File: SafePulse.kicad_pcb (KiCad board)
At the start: 4 copper layers, 40.6 x 20.8 mm, 88 parts, among them IC1 S-35770E01I-K8T2U, J1 Conn_01x03_Male, J2 4208, Q1 FQT7N10L, Q2 BC846A, Q3 MMBT3906, Q4 MMBT3906, U1 TS4061AICT-1.25, U2 74HC14, U3 TLV27L1DBVT, U33 MAX9910EXK+T, U4 CD14538BM

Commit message: added Allan changes
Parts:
- U1: footprint Package_TO_SOT_SMD:SOT-323_SC-70 -> Package_TO_SOT_SMD:SOT-23

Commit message: Updated V1.2.4 board with new JCLPCB number
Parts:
- Q1: footprint Package_TO_SOT_SMD:SOT-223-3_TabPin4 -> Library:SOT230P700X180-4N
- U1: footprint Package_TO_SOT_SMD:SOT-23 -> Library:SOT65P210X110-3N
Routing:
- net GND: track 64.3 -> 63.6 mm
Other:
- copper layers 4 -> 13

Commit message: V1.2.5 boards
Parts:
- Q1: footprint Library:SOT230P700X180-4N -> Package_TO_SOT_SMD:SOT-223-3_TabPin4
- Q2: footprint Package_TO_SOT_SMD:SOT-23 -> Package_TO_SOT_SMD:SOT-323_SC-70_Handsoldering
- U1: footprint Library:SOT65P210X110-3N -> Package_TO_SOT_SMD:SOT-23
- moved Q2 0.51 mm to (149.9, 72.7)
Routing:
- net GND: track 63.6 -> 64.9 mm

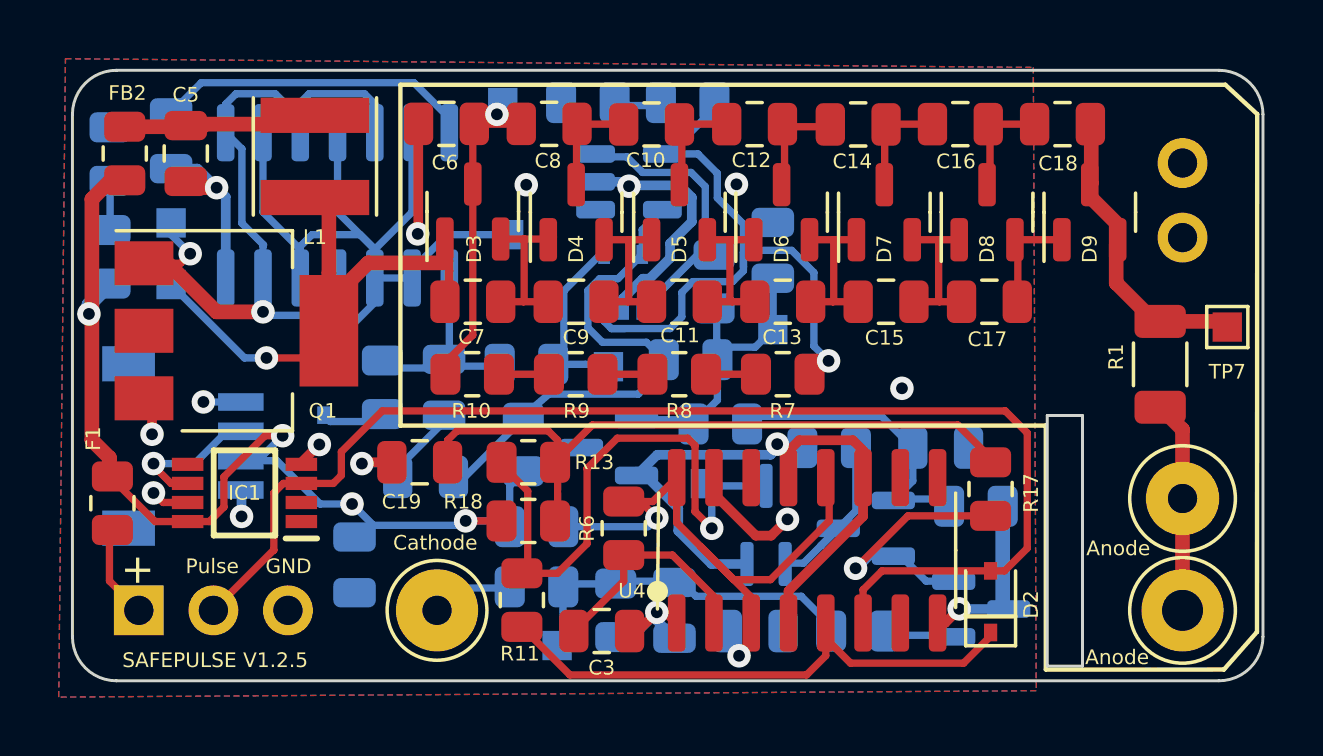
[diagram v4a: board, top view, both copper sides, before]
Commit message: Update layout for SOT-323 for U1 from a SOT-23 footprint
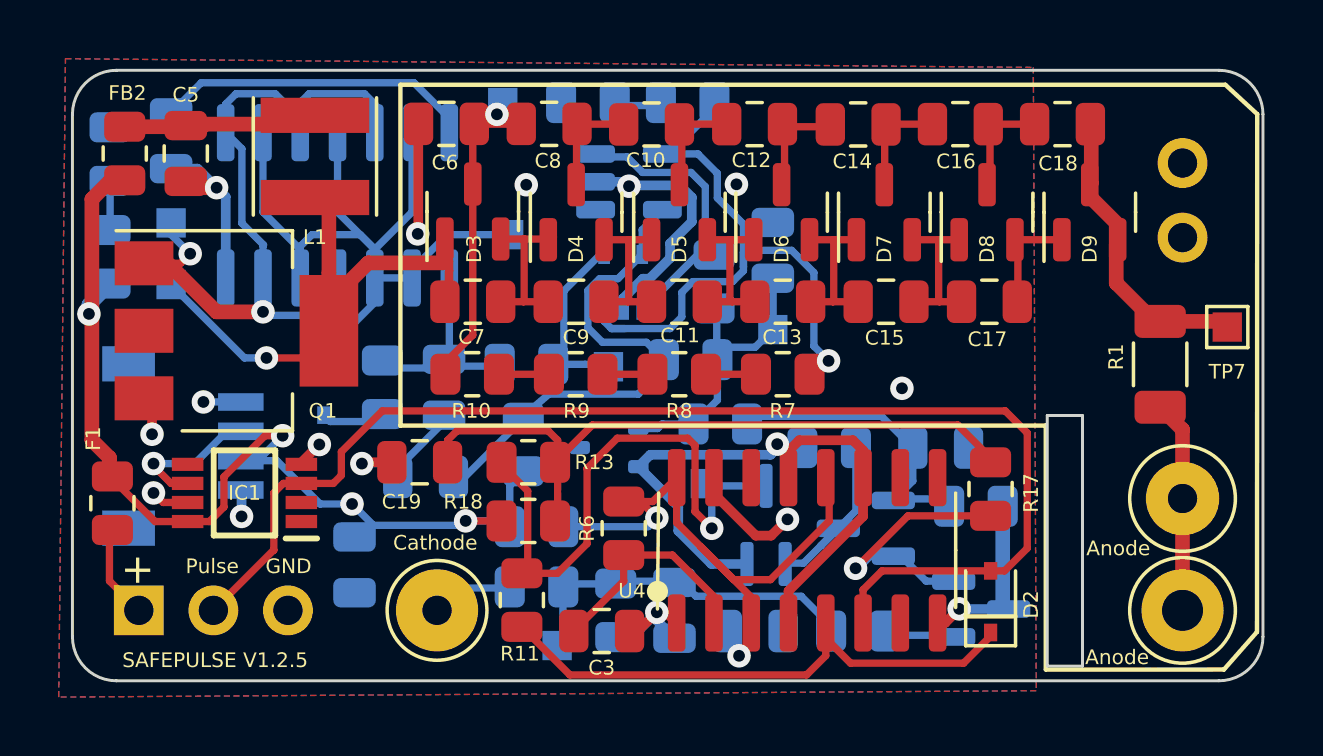
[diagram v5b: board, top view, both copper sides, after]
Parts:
- U1: footprint Package_TO_SOT_SMD:SOT-23 -> Package_TO_SOT_SMD:SOT-323_SC-70
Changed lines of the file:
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@@
 		)
 	)
-	(footprint "Package_TO_SOT_SMD:SOT-23"
+	(footprint "Package_TO_SOT_SMD:SOT-323_SC-70"
 		(layer "B.Cu")
 		(at 144.52 70.02 180)
-		(descr "SOT, 3 Pin (https://www.jedec.org/system/files/docs/to-236h.pdf variant AB), generated with kicad-footprint-generator ipc_gullwing_generator.py")
-		(tags "SOT TO_SOT_SMD")
+		(descr "SOT-323, SC-70")
+		(tags "SOT-323 SC-70")
 		(property "Reference" "U1"
-			(at 0 -2.055 0)
+			(at -0.05 2.25 0)
 			(layer "B.SilkS")
 			(effects
 				(font
-					(size 0.5 0.5)
-					(thickness 0.075)
+					(size 1 1)
+					(thickness 0.15)
 				)
 				(justify mirror)
@@
 		)
 		(property "Value" "TS4061AICT-1.25"
-			(at 0 -2.4 0)
+			(at -0.05 -2.05 0)
 			(layer "B.Fab")
-			(hide yes)
 			(effects
 				(font
@@
 			)
 		)
-		(property "Footprint" "Package_TO_SOT_SMD:SOT-23"
+		(property "Footprint" "Package_TO_SOT_SMD:SOT-323_SC-70"
 			(at 0 0 0)
 			(unlocked yes)
@@
 		(attr smd)
 		(fp_line
-			(start 0.65 1.56)
-			(end 0 1.56)
+			(start 0.73 1.16)
+			(end -0.68 1.16)
 			(stroke
 				(width 0.12)
@@
 		)
 		(fp_line
-			(start 0.65 -1.56)
-			(end 0 -1.56)
+			(start 0.73 0.5)
+			(end 0.73 1.16)
 			(stroke
 				(width 0.12)
@@
 		)
 		(fp_line
-			(start -0.65 1.56)
-			(end 0 1.56)
+			(start 0.73 -1.16)
+			(end 0.73 -0.5)
 			(stroke
 				(width 0.12)
@@
 		)
 		(fp_line
-			(start -0.65 -1.56)
-			(end 0 -1.56)
+			(start 0.73 -1.16)
+			(end -0.68 -1.16)
 			(stroke
 				(width 0.12)
@@
 		(fp_poly
 			(pts
-				(xy -1.1625 1.51) (xy -1.4025 1.84) (xy -0.9225 1.84) (xy -1.1625 1.51)
+				(xy -1.05 1.14) (xy -1.29 1.47) (xy -0.81 1.47) (xy -1.05 1.14)
 			)
 			(stroke
@@
 		)
 		(fp_line
-			(start 1.92 1.7)
-			(end 1.92 -1.7)
+			(start 1.7 1.3)
+			(end -1.7 1.3)
 			(stroke
 				(width 0.05)
@@
 		)
 		(fp_line
-			(start 1.92 -1.7)
-			(end -1.92 -1.7)
+			(start 1.7 -1.3)
+			(end 1.7 1.3)
 			(stroke
 				(width 0.05)
@@
 		)
 		(fp_line
-			(start -1.92 1.7)
-			(end 1.92 1.7)
+			(start -1.7 1.3)
+			(end -1.7 -1.3)
 			(stroke
 				(width 0.05)
@@
 		)
 		(fp_line
-			(start -1.92 -1.7)
-			(end -1.92 1.7)
+			(start -1.7 -1.3)
+			(end 1.7 -1.3)
 			(stroke
 				(width 0.05)
@@
 		)
 		(fp_line
-			(start 0.65 1.45)
-			(end -0.325 1.45)
+			(start 0.67 -1.1)
+			(end 0.67 1.1)
 			(stroke
 				(width 0.1)
@@
 		)
 		(fp_line
-			(start 0.65 -1.45)
-			(end 0.65 1.45)
+			(start -0.18 1.1)
+			(end 0.67 1.1)
 			(stroke
 				(width 0.1)
@@
 		)
 		(fp_line
-			(start -0.325 1.45)
-			(end -0.65 1.125)
+			(start -0.68 0.6)
+			(end -0.18 1.1)
 			(stroke
 				(width 0.1)
@@
 		)
 		(fp_line
-			(start -0.65 1.125)
-			(end -0.65 -1.45)
+			(start -0.68 -1.1)
+			(end 0.67 -1.1)
 			(stroke
 				(width 0.1)
@@
 		)
 		(fp_line
-			(start -0.65 -1.45)
-			(end 0.65 -1.45)
+			(start -0.68 -1.1)
+			(end -0.68 0.6)
 			(stroke
 				(width 0.1)
@@
 		)
 		(fp_text user "${REFERENCE}"
-			(at 0 0 0)
+			(at 0 0 90)
 			(layer "B.Fab")
 			(effects
 				(font
-					(size 0.32 0.32)
-					(thickness 0.05)
+					(size 0.5 0.5)
+					(thickness 0.075)
 				)
 				(justify mirror)
@@
 		)
 		(pad "1" smd roundrect
-			(at -0.9375 0.95 180)
-			(size 1.475 0.6)
+			(at -1 0.65 270)
+			(size 0.45 0.7)
 			(layers "B.Cu" "B.Paste" "B.Mask")
 			(roundrect_rratio 0.25)
@@
 		)
 		(pad "2" smd roundrect
-			(at -0.9375 -0.95 180)
-			(size 1.475 0.6)
+			(at -1 -0.65 270)
+			(size 0.45 0.7)
 			(layers "B.Cu" "B.Paste" "B.Mask")
 			(roundrect_rratio 0.25)
@@
 		)
 		(pad "3" smd roundrect
-			(at 0.9375 0 180)
-			(size 1.475 0.6)
+			(at 1 0 270)
+			(size 0.45 0.7)
 			(layers "B.Cu" "B.Paste" "B.Mask")
 			(roundrect_rratio 0.25)
@@
 			(pintype "power_in")
 		)
-		(model "${KICAD8_3DMODEL_DIR}/Package_TO_SOT_SMD.3dshapes/SOT-23.wrl"
+		(model "${KICAD8_3DMODEL_DIR}/Package_TO_SOT_SMD.3dshapes/SOT-323_SC-70.wrl"
 			(offset
 				(xyz 0 0 0)
@@
 	)
 	(segment
-		(start 146.1625 70.265)
-		(end 145.4575 70.97)
-		(width 0.3302)
-		(layer "B.Cu")
-		(net 3)
-	)
-	(segment
 		(start 137.475 70.565)
 		(end 138.77 69.27)
@@
 	)
 	(segment
-		(start 146.88 72.085)
-		(end 146.88 72.855)
-		(width 0.3302)
-		(layer "B.Cu")
-		(net 3)
-	)
-	(segment
 		(start 132 71.49)
 		(end 131.975 71.465)
@@
 	)
 	(segment
-		(start 146.88 72.855)
-		(end 148.01 73.985)
-		(width 0.3302)
-		(layer "B.Cu")
-		(net 3)
-	)
-	(segment
 		(start 146.146747 75.911747)
 		(end 146.75 76.515)
@@
 	(segment
 		(start 150.025 70.265)
-		(end 146.1625 70.265)
+		(end 145.925 70.265)
 		(width 0.3302)
 		(layer "B.Cu")
@@
 	)
 	(segment
+		(start 146.88 72.855)
+		(end 146.88 72.03)
+		(width 0.3302)
+		(layer "B.Cu")
+		(net 3)
+	)
+	(segment
+		(start 146.88 72.03)
+		(end 145.52 70.67)
+		(width 0.3302)
+		(layer "B.Cu")
+		(net 3)
+	)
+	(segment
 		(start 144.0625 60.965)
 		(end 145.051183 60.965)
@@
 	)
 	(segment
-		(start 148.01 73.985)
-		(end 149.22 73.985)
-		(width 0.3302)
-		(layer "B.Cu")
-		(net 3)
-	)
-	(segment
-		(start 150.08338 70.20662)
-		(end 150.025 70.265)
-		(width 0.3302)
-		(layer "B.Cu")
-		(net 3)
-	)
-	(segment
 		(start 130.5 60.515)
 		(end 129.975 60.515)
@@
 	)
 	(segment
-		(start 145.4575 70.97)
-		(end 145.4575 70.8325)
-		(width 0.3302)
-		(layer "B.Cu")
-		(net 3)
-	)
-	(segment
 		(start 145.051183 60.965)
 		(end 145.2 61.113817)
@@
 	)
 	(segment
+		(start 145.925 70.265)
+		(end 145.52 70.67)
+		(width 0.3302)
+		(layer "B.Cu")
+		(net 3)
+	)
+	(segment
 		(start 132 72.365)
 		(end 132 71.49)
@@
 	)
 	(segment
-		(start 145.765 70.97)
-		(end 146.88 72.085)
+		(start 150.08338 70.20662)
+		(end 150.025 70.265)
 		(width 0.3302)
 		(layer "B.Cu")
@@
 	)
 	(segment
-		(start 146.7125 76.4775)
-		(end 146.75 76.515)
+		(start 148.01 73.985)
+		(end 146.88 72.855)
 		(width 0.3302)
 		(layer "B.Cu")
@@
 	)
 	(segment
-		(start 145.6741 64.265)
-		(end 145 64.9391)
+		(start 146.7125 76.4775)
+		(end 146.75 76.515)
 		(width 0.3302)
 		(layer "B.Cu")
@@
 	)
 	(segment
-		(start 145.4575 70.97)
-		(end 145.765 70.97)
+		(start 145.6741 64.265)
+		(end 145 64.9391)
 		(width 0.3302)
 		(layer "B.Cu")
@@
 	)
 	(segment
+		(start 149.22 73.985)
+		(end 148.01 73.985)
+		(width 0.3302)
+		(layer "B.Cu")
+		(net 3)
+	)
+	(segment
 		(start 150.4 72.665)
 		(end 150.393382 72.665)
@@
 	)
 	(segment
-		(start 148.4125 66.6)
-		(end 148.19 66.3775)
+		(start 146.3308 69.215)
+		(end 146.1758 69.37)
 		(width 0.25)
 		(layer "B.Cu")
@@
 	)
 	(segment
-		(start 150.1 66)
-		(end 150.11 66)
+		(start 147.3995 69.215)
+		(end 146.3308 69.215)
+		(width 0.25)
+		(layer "B.Cu")
+		(net 12)
+	)
+	(segment
+		(start 148.4125 66.6)
+		(end 148.19 66.3775)
 		(width 0.25)
 		(layer "B.Cu")
@@
 	)
 	(segment
-		(start 145.4575 69.07)
-		(end 147.0175 69.07)
+		(start 150.1 66)
+		(end 150.11 66)
 		(width 0.25)
 		(layer "B.Cu")
@@
 	)
 	(segment
-		(start 148.2125 67.024)
-		(end 148.2125 68.402)
+		(start 146.1758 69.37)
+		(end 145.52 69.37)
 		(width 0.25)
 		(layer "B.Cu")
@@
 	)
 	(segment
-		(start 145.72 69.07)
-		(end 145.4575 69.07)
+		(start 148.2125 67.024)
+		(end 148.2125 68.402)
 		(width 0.25)
 		(layer "B.Cu")

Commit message: Updated V21.2.5 boards with C3 to 1.5nF
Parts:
- C3: value 10nF -> 1.5nF
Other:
- copper layers 13 -> 4

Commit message: Updated BOM
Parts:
- C3: value 1.5nF -> 1nF
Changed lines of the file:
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@@
 			)
 		)
-		(property "Value" "1.5nF"
+		(property "Value" "1nF"
 			(at 0 1.68 180)
 			(layer "F.Fab")
